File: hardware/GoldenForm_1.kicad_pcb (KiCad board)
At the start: 4 copper layers, 60 x 45.3 mm, 60 parts, among them IC1 UVLO, J1 1140084168, J2 Conn_01x02_Pin, J3 USB4105-GF-A, J4 Conn_01x04_Pin, J5 Conn_01x02_Pin, M1 MountingHole x 4, U1 ESP32-S3-WROOM-1, U2 BNO055, U3 Buck_Boost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

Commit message: need to sort DRCs
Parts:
- moved J2 57.5 mm to (125.7, 67.0)
- moved D9 10.7 mm to (124.9, 59.0), turned to 180 degrees
- moved R8 9.96 mm to (83.3, 64.4), turned to 90 degrees
- moved R21 7.55 mm to (105.3, 94.3), turned to 180 degrees
- moved R20 6.55 mm to (120.3, 64.7), turned to 0 degrees
- moved R9 6.31 mm to (110.9, 94.3), turned to 180 degrees
- moved J5 4.71 mm to (125.2, 61.6), turned to 90 degrees
- moved R6 4.23 mm to (77.3, 72.6)
- moved R7 4.23 mm to (77.2, 76.8)
- moved J3 4.23 mm to (71.0, 74.8)
- moved U4 3.72 mm to (122.0, 61.3), turned to 0 degrees
- moved R3 2.71 mm to (88.5, 73.5)
- moved D8 2.52 mm to (103.9, 84.9)
- moved S5 2.52 mm to (105.5, 89.4)
- moved D4 2.52 mm to (110.3, 84.6), turned to 180 degrees
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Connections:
- C4 pad 2: Net-(U2-VDDIO) -> V_DD
- R8 pad 1: Net-(U2-VDDIO) -> V_DD
- U1 pad 16: SYNC_BUTTON -> unconnected-(U1-IO46-Pad16)
- U1 pad 20: unconnected-(U1-IO12-Pad20) -> SYNC_BUTTON
- U1 pad 21: unconnected-(U1-IO13-Pad21) -> ST_BUTTON
- U1 pad 26: ST_BUTTON -> HAPTIC
- U1 pad 31: HAPTIC -> unconnected-(U1-IO38-Pad31)
- U2 pad 28: Net-(U2-VDDIO) -> V_DD
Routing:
- net EN_PIN: track 0.00 -> 33.3 mm, vias 0 -> 2
- net UART_TX: track 0.00 -> 25.2 mm, vias 0 -> 2
- net BOOT_PIN: track 0.00 -> 24.6 mm, vias 0 -> 2
- net ST_BUTTON: track 0.00 -> 24.6 mm
- net UART_RX: track 0.00 -> 24.5 mm
- net GND: track 13.4 -> 36.4 mm, vias 30 -> 42
- net SYNC_BUTTON: track 0.00 -> 20.8 mm
- net HAPTIC: track 0.00 -> 16.2 mm
- net Net-(D9-A): track 0.00 -> 5.35 mm
- net IO3: track 0.00 -> 4.21 mm
- net Net-(S1-NO_1): track 0.00 -> 4.06 mm
- net Net-(S3-NO_1): track 0.00 -> 3.95 mm
- net Net-(S5-NO_1): track 0.00 -> 2.87 mm
- net Net-(S4-NO_1): track 0.00 -> 2.84 mm
- net Net-(U2-~{RESET}): track 0.00 -> 2.47 mm
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
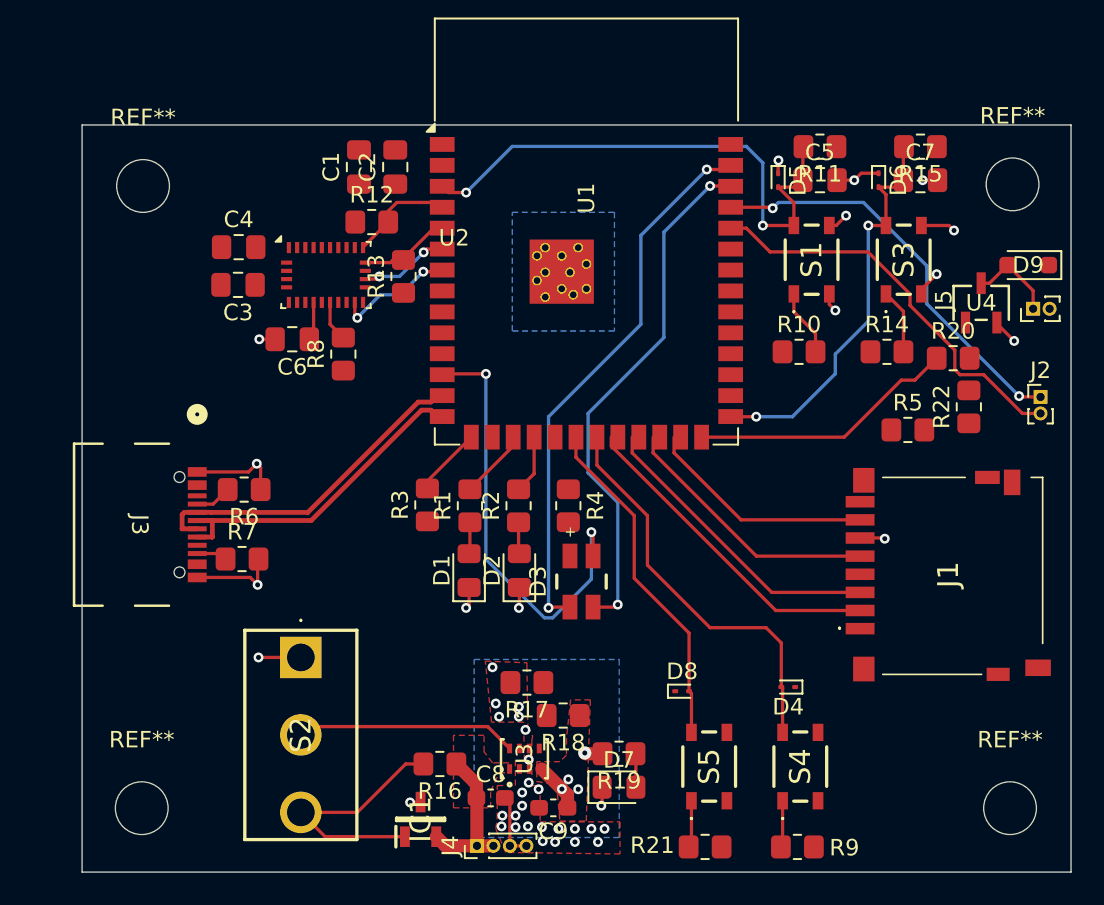
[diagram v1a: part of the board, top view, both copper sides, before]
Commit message: added caps for vdd sd, added esd for usbc, fixed i2c addr from bno
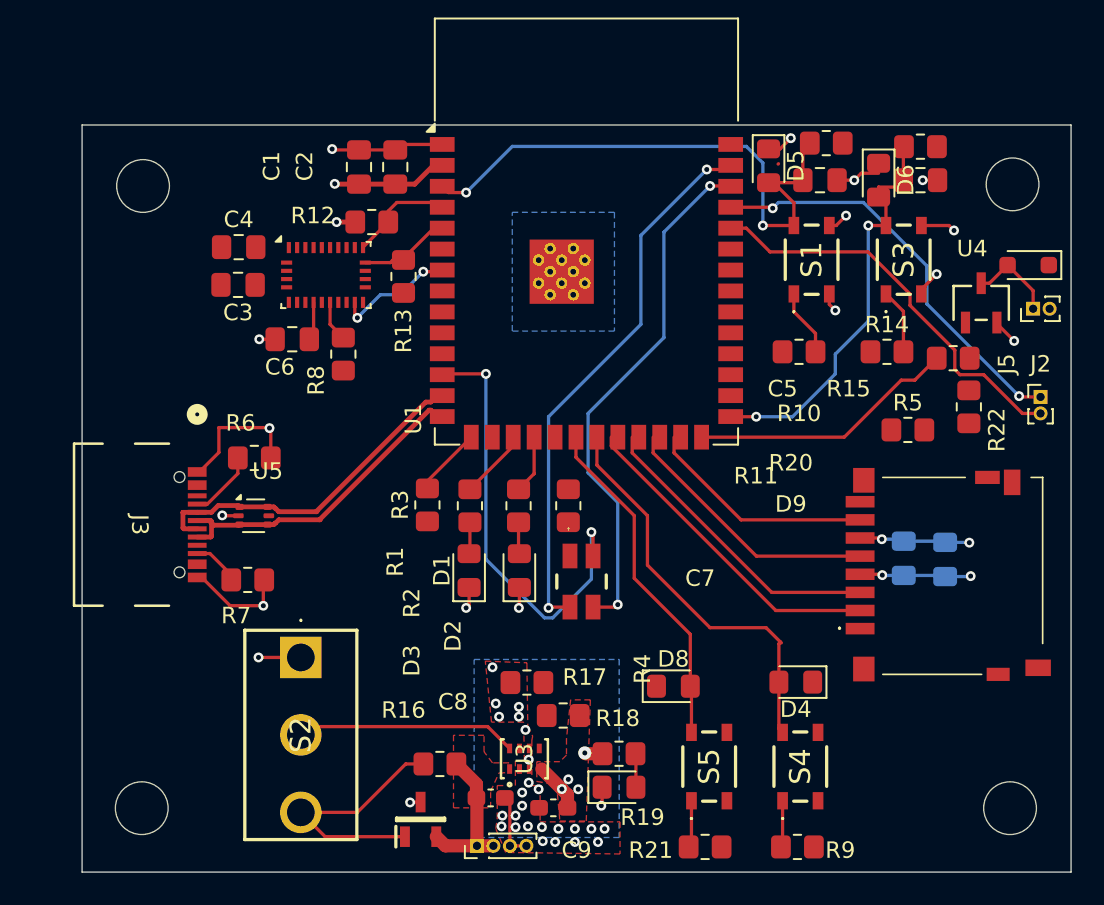
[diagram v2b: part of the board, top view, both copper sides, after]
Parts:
- added C10: 22uF, Capacitor_SMD:C_0805_2012Metric_Pad1.18x1.45mm_HandSolder, B.Cu at (119.9, 76.9)
- added C11: 0.1uF, Capacitor_SMD:C_0805_2012Metric_Pad1.18x1.45mm_HandSolder, B.Cu at (117.3, 76.8)
- added U5: USBLC6-2P6, Package_TO_SOT_SMD:SOT-666, F.Cu at (77.9, 74.2)
- D4, D5, D6, D8: footprint Diode_SMD:D_SOD-923 -> Diode_SMD:D_0805_2012Metric_Pad1.15x1.40mm_HandSolder
- moved R6 2.02 mm to (78.0, 70.7)
- moved R7 1.31 mm to (77.5, 78.1)
- moved D5 1.05 mm to (109.2, 53.0)
- moved D8 0.61 mm to (103.4, 84.5)
- moved D4 0.55 mm to (110.8, 84.3)
- moved R11 0.44 mm to (112.7, 51.6)
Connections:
- net D+ renamed USB_D+
- net D- renamed USB_D-
- U1 pad 6: I2C_ADDR -> unconnected-(U1-IO6-Pad6)
- U2 pad 17: I2C_ADDR -> GND
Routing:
- net GND: track 36.4 -> 53.9 mm, vias 42 -> 45
- net V_DD: track 4.10 -> 19.1 mm, vias 4 -> 8
- net I2C_ADDR: track 5.42 -> 0.00 mm, vias 2 -> 0
- net EN_PIN: track 33.3 -> 35.5 mm
- net Net-(J3-CC1): track 2.21 -> 4.18 mm
- net Net-(J3-CC2): track 1.86 -> 3.38 mm
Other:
- board text added: "${REFERENCE}"

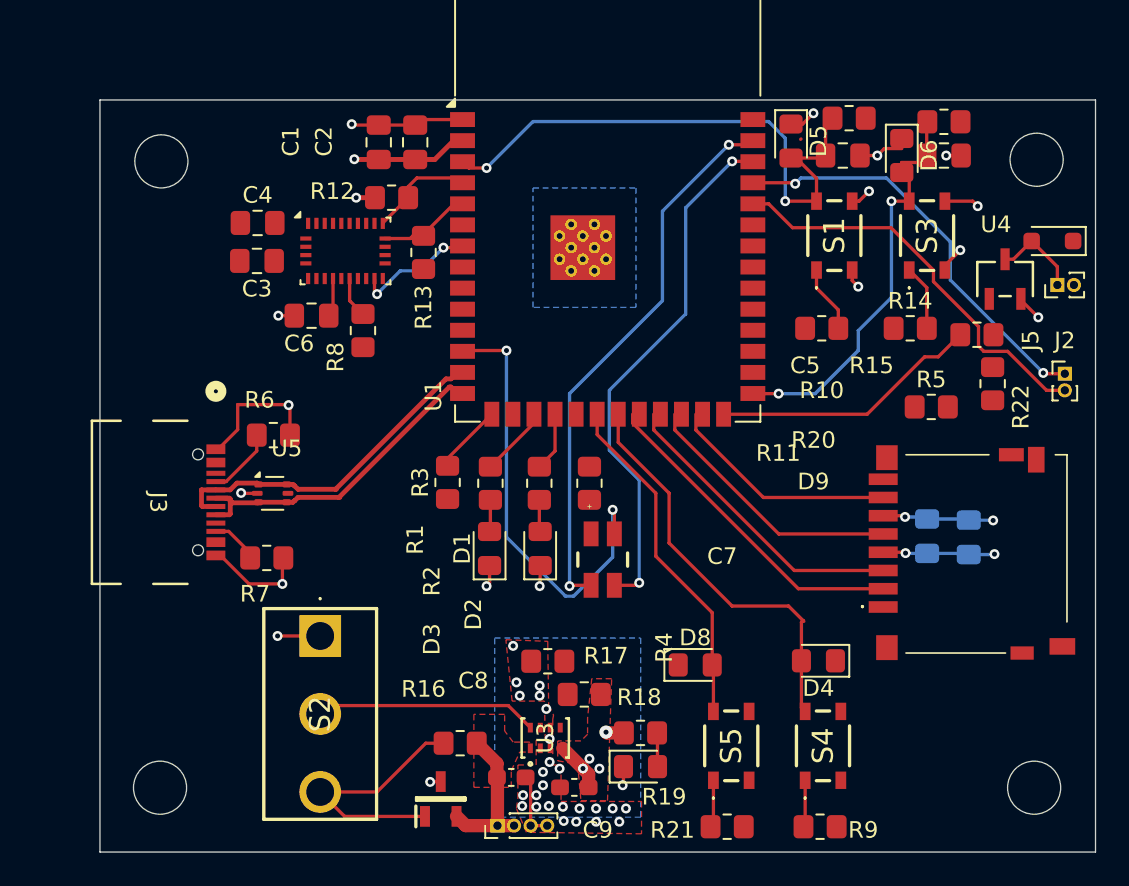
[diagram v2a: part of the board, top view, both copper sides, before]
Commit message: 0 DRC errors. Need to do silkscreen
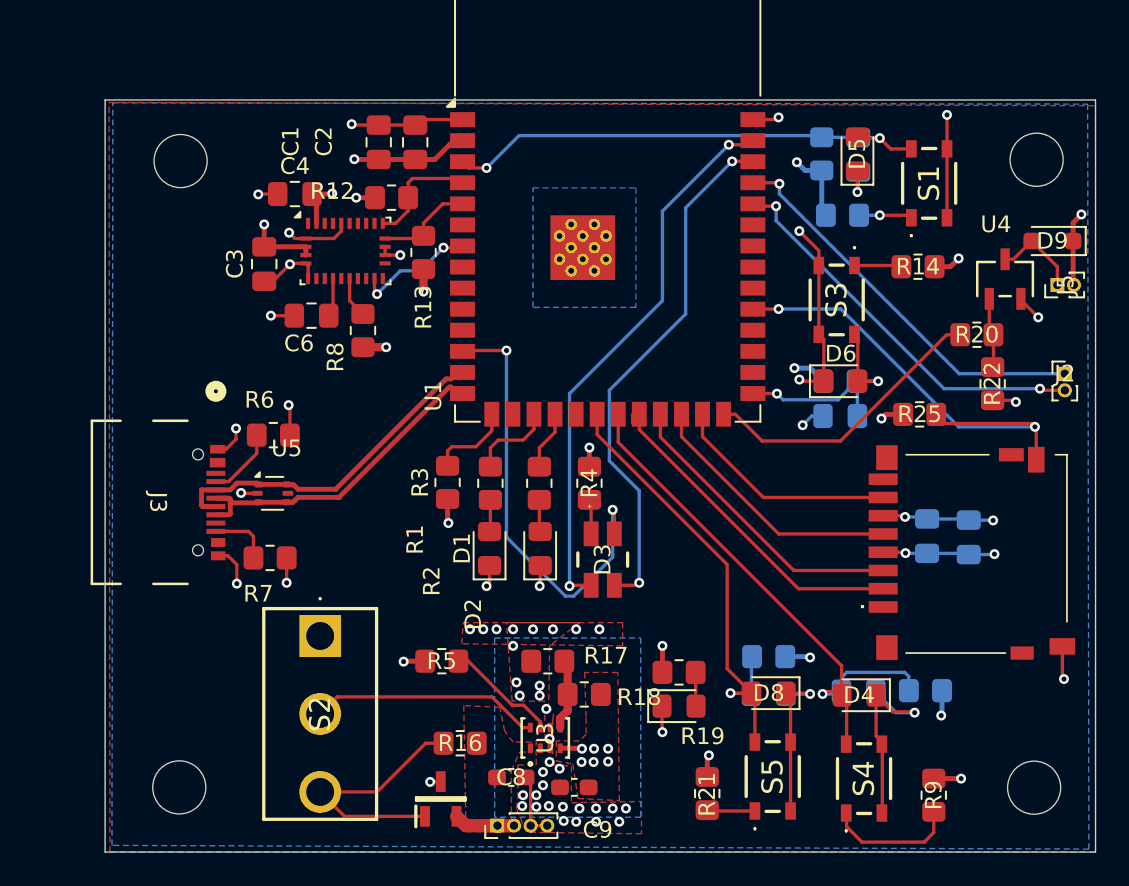
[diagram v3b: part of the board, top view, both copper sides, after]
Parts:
- added C12: 1uF, Capacitor_SMD:C_0805_2012Metric_Pad1.18x1.45mm_HandSolder, B.Cu at (113.2, 86.2)
- added C13: 1uF, Capacitor_SMD:C_0805_2012Metric_Pad1.18x1.45mm_HandSolder, B.Cu at (107.8, 86.3)
- added R23: 10k, Resistor_SMD:R_0805_2012Metric_Pad1.20x1.40mm_HandSolder, B.Cu at (117.2, 86.1)
- added R24: 10k, Resistor_SMD:R_0805_2012Metric_Pad1.20x1.40mm_HandSolder, B.Cu at (107.8, 84.0)
- added R25: 10k, Resistor_SMD:R_0805_2012Metric_Pad1.20x1.40mm_HandSolder, F.Cu at (116.9, 69.5)
- C5, C7, R10, R11, R15: moved to B.Cu
- moved R5 33.2 mm to (88.1, 84.3)
- moved C7 16.9 mm to (112.1, 69.5), turned to 180 degrees
- moved R15 16.8 mm to (112.1, 67.5), turned to 0 degrees
- moved D6 14.1 mm to (112.2, 67.5), turned to 0 degrees
- moved R9 7.11 mm to (117.8, 92.4), turned to -90 degrees
- moved R10 6.93 mm to (112.2, 57.5)
- moved S3 6.69 mm to (111.9, 62.5), turned to -90 degrees
- moved S1 6.53 mm to (117.5, 55.5)
- moved D8 4.74 mm to (107.8, 86.2), turned to 180 degrees
- moved D7 4.32 mm to (102.4, 87.0)
- moved R19 4.32 mm to (102.4, 85.0)
- moved D5 4.07 mm to (113.2, 53.8), turned to 90 degrees
- moved R14 3.74 mm to (116.8, 60.5), turned to 180 degrees
- moved D4 3.21 mm to (113.2, 86.4)
- moved S4 3.17 mm to (113.5, 91.4)
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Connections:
- J1 pad CD2: unconnected-(J1-CARD_DETECT_SW_2-PadCD2) -> GND
- J3 pad A4-B9: V_BUS -> unconnected-(J3-VBUS-PadA4-B9)
- J3 pad B4-A9: V_BUS -> unconnected-(J3-VBUS-PadB4-A9)
- R5 pad 2: SD_DETECT -> Net-(U3-MODE)
- U1 pad 19: SD_DETECT -> unconnected-(U1-IO11-Pad19)
- U1 pad 28: PSRAM -> unconnected-(U1-IO35-Pad28)
- U1 pad 29: PSRAM -> unconnected-(U1-IO36-Pad29)
- U1 pad 30: PSRAM -> unconnected-(U1-IO37-Pad30)
- U1 pad 31: unconnected-(U1-IO38-Pad31) -> SD_DETECT
- U1 pad 32: JTAG -> unconnected-(U1-IO39-Pad32)
- U1 pad 33: JTAG -> unconnected-(U1-IO40-Pad33)
- U1 pad 34: JTAG -> unconnected-(U1-IO41-Pad34)
- U1 pad 35: JTAG -> unconnected-(U1-IO42-Pad35)
- U3 pad 7: MODE -> Net-(U3-MODE)
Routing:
- net GND: track 53.9 -> 94.9 mm, vias 45 -> 61
- net V_DD: track 19.1 -> 51.8 mm, vias 8 -> 27
- net SD_DETECT: track 0.00 -> 28.2 mm, vias 0 -> 2
- net BOOT_PIN: track 24.6 -> 14.6 mm
- net ST_BUTTON: track 24.7 -> 33.9 mm, vias 0 -> 1
- net SYNC_BUTTON: track 21.0 -> 28.5 mm, vias 0 -> 1
- net Net-(U3-MODE): track 0.00 -> 6.80 mm
- net EN_PIN: track 35.5 -> 29.7 mm
- net V_Bat: track 9.16 -> 3.67 mm
- net Net-(S4-NO_1): track 2.84 -> 8.09 mm
- net FB: track 0.00 -> 4.27 mm
- net Net-(U4-G): track 0.00 -> 4.24 mm
- net Net-(D3-Pad1): track 0.00 -> 2.09 mm
- net HAPTIC: track 16.2 -> 17.6 mm
- net UART_TX: track 25.2 -> 23.9 mm, vias 2 -> 1
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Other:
- board size 60 x 45.3 mm -> 59.7 x 45.3 mm
- board text removed: "${REFERENCE}"

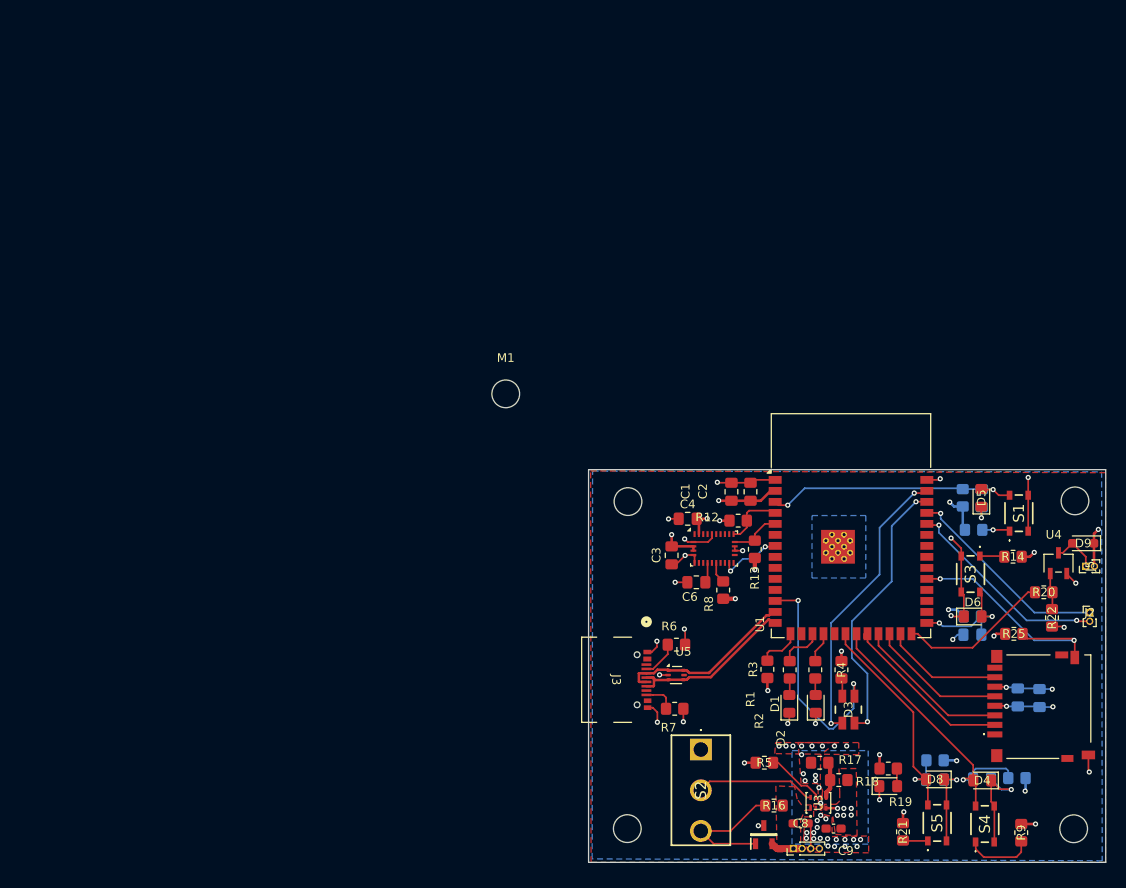
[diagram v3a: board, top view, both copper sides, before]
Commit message: added silkscreen, logo, etc.
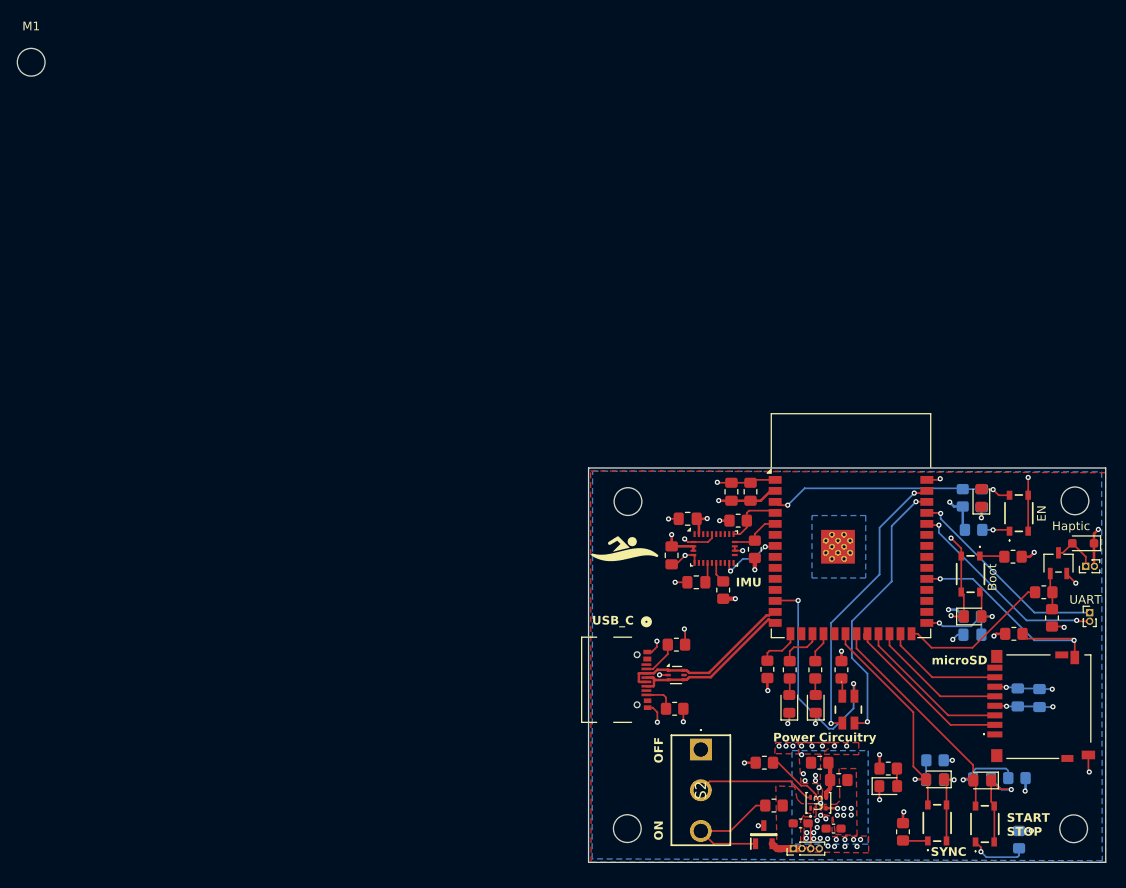
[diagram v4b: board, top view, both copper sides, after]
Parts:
- R9: moved to B.Cu
- moved M1 66.8 mm to (3.48, 3.48)
- moved R9 0.84 mm to (117.5, 93.2)
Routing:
- net Net-(S4-NO_1): track 8.09 -> 6.95 mm, vias 0 -> 1
- net V_DD: track 51.8 -> 51.0 mm
- net GND: track 94.9 -> 94.3 mm
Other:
- board size 59.7 x 45.3 mm -> 59.7 x 45.5 mm
- board text added: "Boot"
- board text added: "EN"
- board text added: "GoldenForm - V1 Atharva Bhide Armaan Kanchan Nikhil Chaudhary Aakash Bathini"
- board text added: "Haptic"
- board text added: "IMU"
- board text added: "OFF"
- board text added: "ON"
- board text added: "Power Circuitry"
- board text added: "START STOP"
- board text added: "SYNC"
- board text added: "UART"
- board text added: "USB_C"
- board text added: "microSD"

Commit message: CDR updates
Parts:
- removed M1: MountingHole x 4, MountingHole:MountingHole_3.2mm_M3
- J2: footprint Connector_PinHeader_1.00mm:PinHeader_1x02_P1.00mm_Vertical -> Connector_PinHeader_2.54mm:PinHeader_1x02_P2.54mm_Vertical
- J4: footprint Connector_PinHeader_1.00mm:PinHeader_1x04_P1.00mm_Vertical -> Connector_PinHeader_2.54mm:PinHeader_1x04_P2.54mm_Vertical
- moved J3 3.09 mm to (70.2, 71.8)
- moved R6 3.09 mm to (77.2, 67.7)
- moved U5 3.09 mm to (77.2, 71.2)
- moved R7 2.85 mm to (77.8, 75.2)
- moved J2 1.58 mm to (125.7, 65.4)
- moved C9 0.43 mm to (96.1, 91.5)
- moved IC1 0.41 mm to (87.7, 92.5)
- moved J4 0.09 mm to (91.5, 94.3)
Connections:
- J3 pad B4-A9: unconnected-(J3-VBUS-PadB4-A9) -> V_BUS
- U5 pad 5: unconnected-(U5-VBUS-Pad5) -> V_BUS
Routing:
- net V_Bat: track 3.67 -> 9.77 mm
- net V_BUS: track 0.00 -> 6.02 mm, vias 0 -> 2
- net USB_D-: track 20.9 -> 18.9 mm
- net GND: track 94.3 -> 92.7 mm, vias 61 -> 53
- net USB_D+: track 20.2 -> 18.8 mm
- net UART_TX: track 23.9 -> 24.6 mm, vias 1 -> 2
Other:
- board size 59.7 x 45.5 mm -> 59.7 x 46.1 mm
